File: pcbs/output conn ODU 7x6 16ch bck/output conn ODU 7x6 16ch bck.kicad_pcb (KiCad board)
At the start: 4 copper layers, 72 x 114 mm, 43 parts, among them J1 ODU-MAC_Zero_6x7, J2 Conn_02x25_Odd_Even, J3 Conn_02x25_Odd_Even

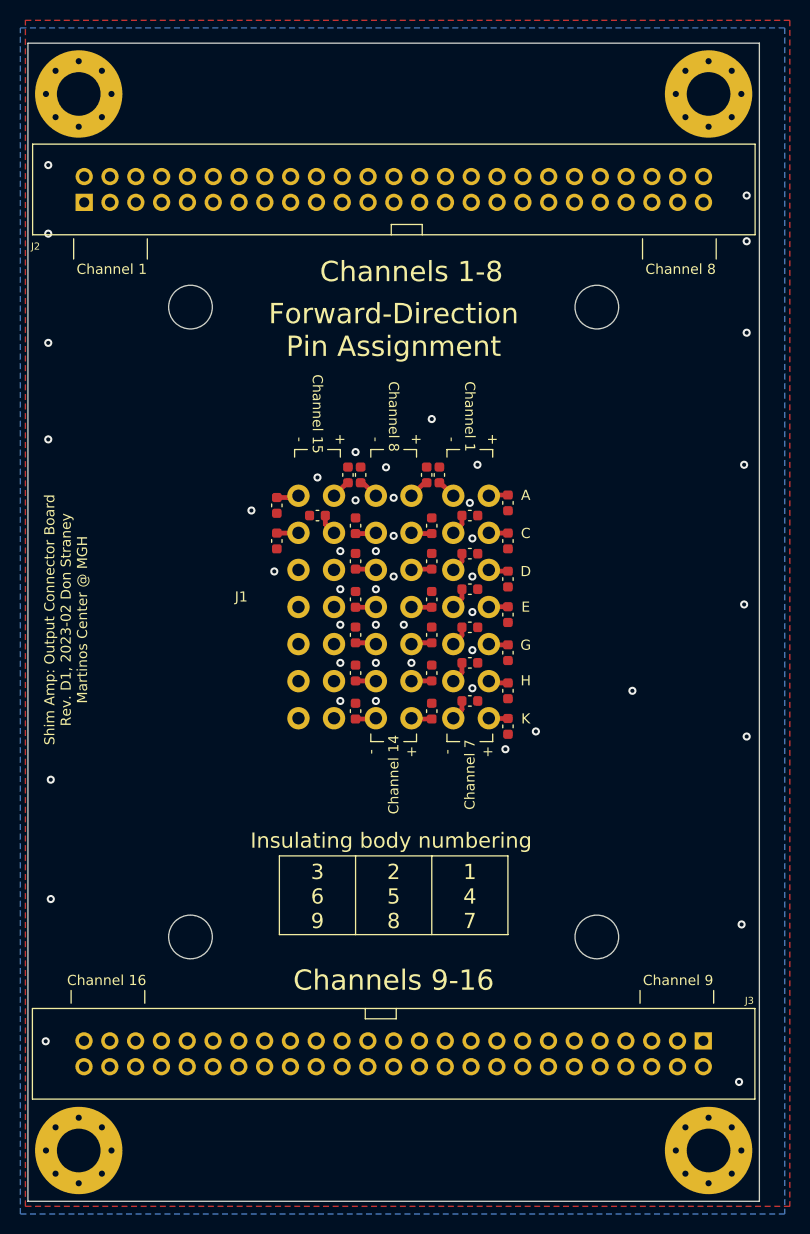
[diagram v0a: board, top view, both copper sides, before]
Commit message: Corrected amp board ADC op-amp, created ODU connector 6x7 board
Pared down list of ADC driver op-amps to list of ones tested
Minor fixes to ODU 6x7 connector board (forward-pinned)
Created duplicate of ODU 6x7 connector board, for reverse-pinned
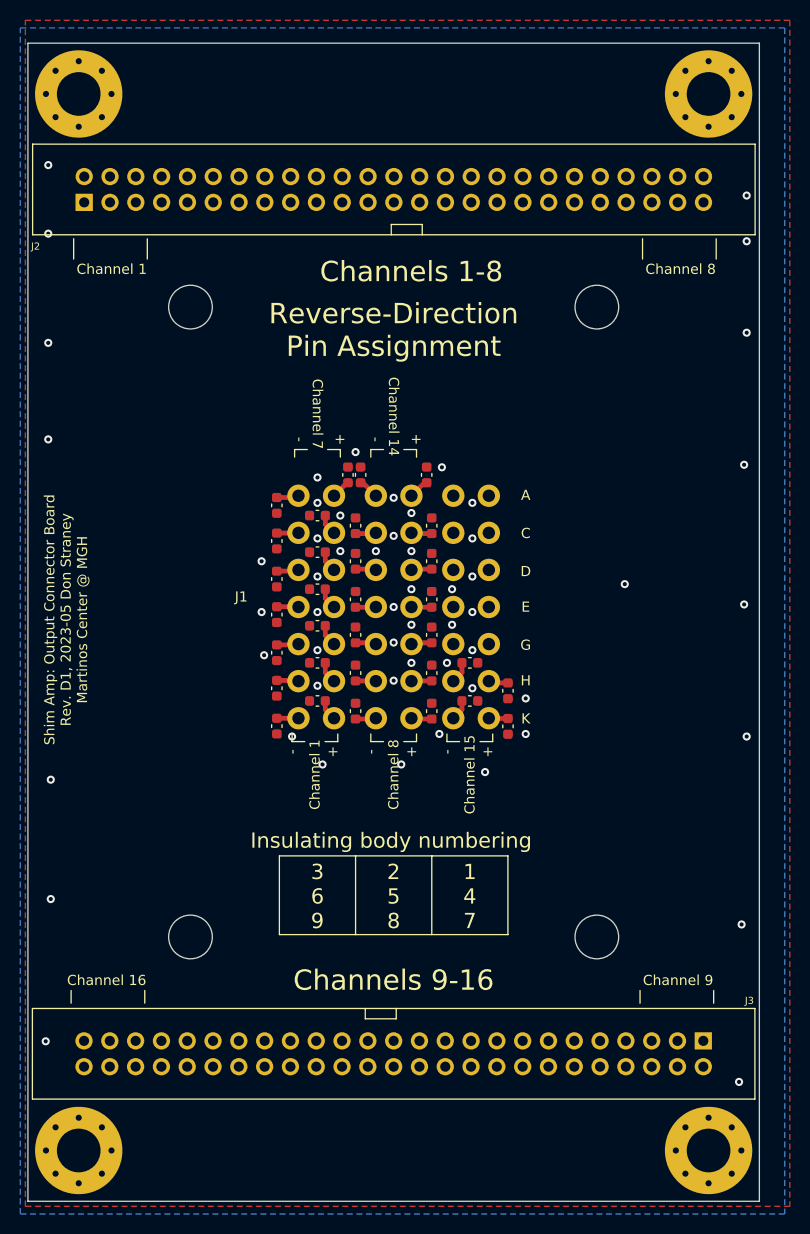
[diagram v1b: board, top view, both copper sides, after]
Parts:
- moved C2 29.5 mm to (97.5, 130.7), turned to -90 degrees
- moved C13 29.3 mm to (104.5, 106.0), turned to 90 degrees
- moved C29 29.3 mm to (120.2, 130.8), turned to -90 degrees
- moved C1 27.1 mm to (101.5, 128.2), turned to 180 degrees
- moved C14 27.0 mm to (97.5, 109.0), turned to -90 degrees
- moved C30 27.0 mm to (116.5, 128.2), turned to 0 degrees
- moved C4 25.5 mm to (97.5, 127.0), turned to -90 degrees
- moved C11 25.5 mm to (101.5, 110.0), turned to 180 degrees
- moved C31 25.5 mm to (120.2, 127.2), turned to -90 degrees
- moved C15 23.3 mm to (112.8, 129.2)
- moved C16 23.3 mm to (105.2, 129.2)
- moved C27 23.3 mm to (112.2, 106.0)
- moved C28 23.3 mm to (105.8, 106.0)
- moved C12 22.5 mm to (97.5, 112.5), turned to -90 degrees
- moved C32 22.5 mm to (116.5, 124.5), turned to 0 degrees
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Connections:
- J1 pad 1: /P1+ -> unconnected-(J1-Pad1)
- J1 pad 10: /P5- -> unconnected-(J1-Pad10)
- J1 pad 11: /P6+ -> /P16+
- J1 pad 12: /P6- -> /P16-
- J1 pad 13: /P7+ -> /P15+
- J1 pad 14: /P7- -> /P15-
- J1 pad 15: /P8+ -> /P14+
- J1 pad 16: /P8- -> /P14-
- J1 pad 17: /P9+ -> /P13+
- J1 pad 18: /P9- -> /P13-
- J1 pad 19: /P10+ -> /P12+
- J1 pad 2: /P1- -> unconnected-(J1-Pad2)
- J1 pad 20: /P10- -> /P12-
- J1 pad 23: /P12+ -> /P10+
- J1 pad 24: /P12- -> /P10-
- J1 pad 25: /P13+ -> /P9+
- J1 pad 26: /P13- -> /P9-
- J1 pad 27: /P14+ -> /P8+
- J1 pad 28: /P14- -> /P8-
- J1 pad 29: /P15+ -> /P7+
- J1 pad 3: /P2+ -> unconnected-(J1-Pad3)
- J1 pad 30: /P15- -> /P7-
- J1 pad 31: /P16+ -> /P6+
- J1 pad 32: /P16- -> /P6-
- J1 pad 33: unconnected-(J1-Pad33) -> /P5+
- J1 pad 34: unconnected-(J1-Pad34) -> /P5-
- J1 pad 35: unconnected-(J1-Pad35) -> /P4+
- J1 pad 36: unconnected-(J1-Pad36) -> /P4-
- J1 pad 37: unconnected-(J1-Pad37) -> /P3+
- J1 pad 38: unconnected-(J1-Pad38) -> /P3-
- J1 pad 39: unconnected-(J1-Pad39) -> /P2+
- J1 pad 4: /P2- -> unconnected-(J1-Pad4)
- J1 pad 40: unconnected-(J1-Pad40) -> /P2-
- J1 pad 41: unconnected-(J1-Pad41) -> /P1+
- J1 pad 42: unconnected-(J1-Pad42) -> /P1-
- J1 pad 5: /P3+ -> unconnected-(J1-Pad5)
- J1 pad 6: /P3- -> unconnected-(J1-Pad6)
- J1 pad 7: /P4+ -> unconnected-(J1-Pad7)
- J1 pad 8: /P4- -> unconnected-(J1-Pad8)
- J1 pad 9: /P5+ -> unconnected-(J1-Pad9)
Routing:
- net /P13-: track 54.2 -> 113.2 mm
- net /P14-: track 47.0 -> 101.3 mm
- net /P13+: track 52.1 -> 103.7 mm
- net /P14+: track 44.9 -> 88.3 mm
- net /P12-: track 51.6 -> 93.7 mm
- net /P12+: track 47.6 -> 87.5 mm
- net /P8-: track 54.8 -> 89.4 mm
- net /P8+: track 50.8 -> 81.5 mm
- net /P11+: track 60.7 -> 84.9 mm
- net /P7-: track 77.3 -> 53.6 mm
- net /P7+: track 72.1 -> 49.3 mm
- net /P11-: track 70.0 -> 91.1 mm
- net /P6-: track 75.5 -> 54.8 mm
- net /P15+: track 68.2 -> 51.0 mm
- net /P6+: track 70.3 -> 53.7 mm
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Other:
- board text added: "Reverse-Direction Pin Assignment"
- board text added: "Shim Amp: Output Connector Board Rev. D1, 2023-05 Don Straney Martinos Center @ MGH"
- board text removed: "Forward-Direction Pin Assignment"
- board text removed: "Shim Amp: Output Connector Board Rev. D1, 2023-02 Don Straney Martinos Center @ MGH"

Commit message: Added extra channels to fwd and bck boards
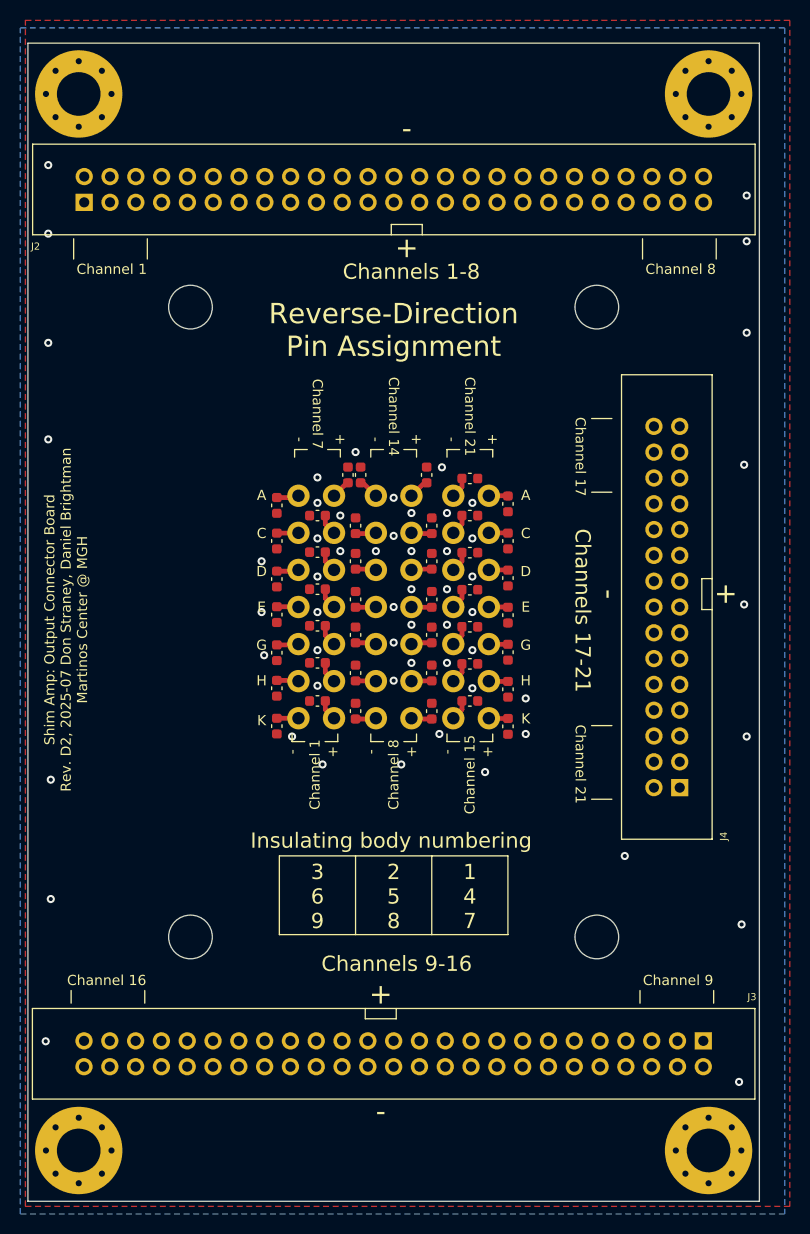
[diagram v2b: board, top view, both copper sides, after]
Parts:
- added C33: C, Capacitor_SMD:C_0603_1608Metric, F.Cu at (120.2, 123.5)
- added C34: C, Capacitor_SMD:C_0603_1608Metric, F.Cu at (116.5, 121.0)
- added C35: C, Capacitor_SMD:C_0603_1608Metric, F.Cu at (120.2, 119.8)
- added C36: C, Capacitor_SMD:C_0603_1608Metric, F.Cu at (116.5, 117.3)
- added C37: C, Capacitor_SMD:C_0603_1608Metric, F.Cu at (120.2, 116.2)
- added C38: C, Capacitor_SMD:C_0603_1608Metric, F.Cu at (116.5, 113.7)
- added C39: C, Capacitor_SMD:C_0603_1608Metric, F.Cu at (120.2, 112.5)
- added C40: C, Capacitor_SMD:C_0603_1608Metric, F.Cu at (116.5, 110.0)
- added C41: C, Capacitor_SMD:C_0603_1608Metric, F.Cu at (120.2, 108.8)
- added C42: C, Capacitor_SMD:C_0603_1608Metric, F.Cu at (116.5, 106.3)
- added J4: Conn_02x15_Odd_Even, shim_amp_linear:PinHeader_2x15_P2.54mm_Vertical_Shrouded, F.Cu at (137.2, 136.8)
- J2, J3: footprint Martinos_std:PinHeader_2x25_P2.54mm_Vertical_Shrouded -> shim_amp_linear:PinHeader_2x25_P2.54mm_Vertical_Shrouded
- moved C31 0.15 mm to (120.2, 127.1)
- moved C32 0.10 mm to (116.5, 124.6)
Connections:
- J1 pad 1: unconnected-(J1-Pad1) -> /P21+
- J1 pad 10: unconnected-(J1-Pad10) -> /P17-
- J1 pad 2: unconnected-(J1-Pad2) -> /P21-
- J1 pad 3: unconnected-(J1-Pad3) -> /P20+
- J1 pad 4: unconnected-(J1-Pad4) -> /P20-
- J1 pad 5: unconnected-(J1-Pad5) -> /P19+
- J1 pad 6: unconnected-(J1-Pad6) -> /P19-
- J1 pad 7: unconnected-(J1-Pad7) -> /P18+
- J1 pad 8: unconnected-(J1-Pad8) -> /P18-
- J1 pad 9: unconnected-(J1-Pad9) -> /P17+
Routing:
- net /P17-: track 0.00 -> 31.3 mm
- net /P18-: track 0.00 -> 29.8 mm
- net /P17+: track 0.00 -> 29.5 mm
- net /P19-: track 0.00 -> 28.4 mm
- net /P20-: track 0.00 -> 28.0 mm
- net /P21-: track 0.00 -> 27.9 mm
- net /P18+: track 0.00 -> 27.9 mm
- net /P19+: track 0.00 -> 27.3 mm
- net /P21+: track 0.00 -> 26.6 mm
- net /P20+: track 0.00 -> 26.2 mm
- net /P8+: track 81.5 -> 104.7 mm
- net /P8-: track 89.4 -> 112.6 mm
- net GND: vias 57 -> 59
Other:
- board text added: "Channel 17"
- board text added: "Channel 21"
- board text added: "Channels 17-21"
- board text added: "Shim Amp: Output Connector Board Rev. D2, 2025-07 Don Straney, Daniel Brightman Martinos Center @ MGH"
- board text removed: "Shim Amp: Output Connector Board Rev. D1, 2023-05 Don Straney Martinos Center @ MGH"

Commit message: Added ODU footprints
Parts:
- J1: footprint Don:ODU-MAC_Zero_6x7 -> shim_amp_linear:ODU-MAC_Zero_6x7_bck
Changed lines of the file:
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@@
 		)
 	)
-	(footprint "Don:ODU-MAC_Zero_6x7"
+	(footprint "shim_amp_linear:ODU-MAC_Zero_6x7_bck"
 		(layer "B.Cu")
 		(at 109 119 180)
@@
 			)
 		)
-		(property "Footprint" "Don:ODU-MAC_Zero_6x7"
-			(at 0 0 180)
+		(property "Footprint" "shim_amp_linear:ODU-MAC_Zero_6x7_bck"
+			(at 0 0 0)
 			(layer "F.Fab")
 			(hide yes)
@@
 		)
 		(property "Datasheet" ""
-			(at 0 0 180)
+			(at 0 0 0)
 			(layer "F.Fab")
 			(hide yes)
@@
 		)
 		(property "Description" ""
-			(at 0 0 180)
+			(at 0 0 0)
 			(layer "F.Fab")
 			(hide yes)
@@
 			)
 		)
-		(fp_text user "Rounded top"
-			(at 0 17 0)
+		(fp_text user "+/- 20 mm X,-29.52 mm +32.48 mm Y"
+			(at 0 22.8 0)
 			(layer "Eco1.User")
 			(effects
 				(font
 					(size 1 1)
-					(thickness 0.15)
+					(thickness 0.05)
 				)
 			)
@@
 			)
 		)
-		(fp_text user "+/- 20 mm X,-29.52 mm +32.48 mm Y"
-			(at 0 22.8 0)
+		(fp_text user "Rounded top"
+			(at 0 17 0)
 			(layer "Eco1.User")
 			(effects
 				(font
 					(size 1 1)
-					(thickness 0.05)
+					(thickness 0.15)
 				)
 			)
